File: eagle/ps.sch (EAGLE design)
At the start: 12 parts, among them J1 PIN2F061.100, J2 PIN2F061.100

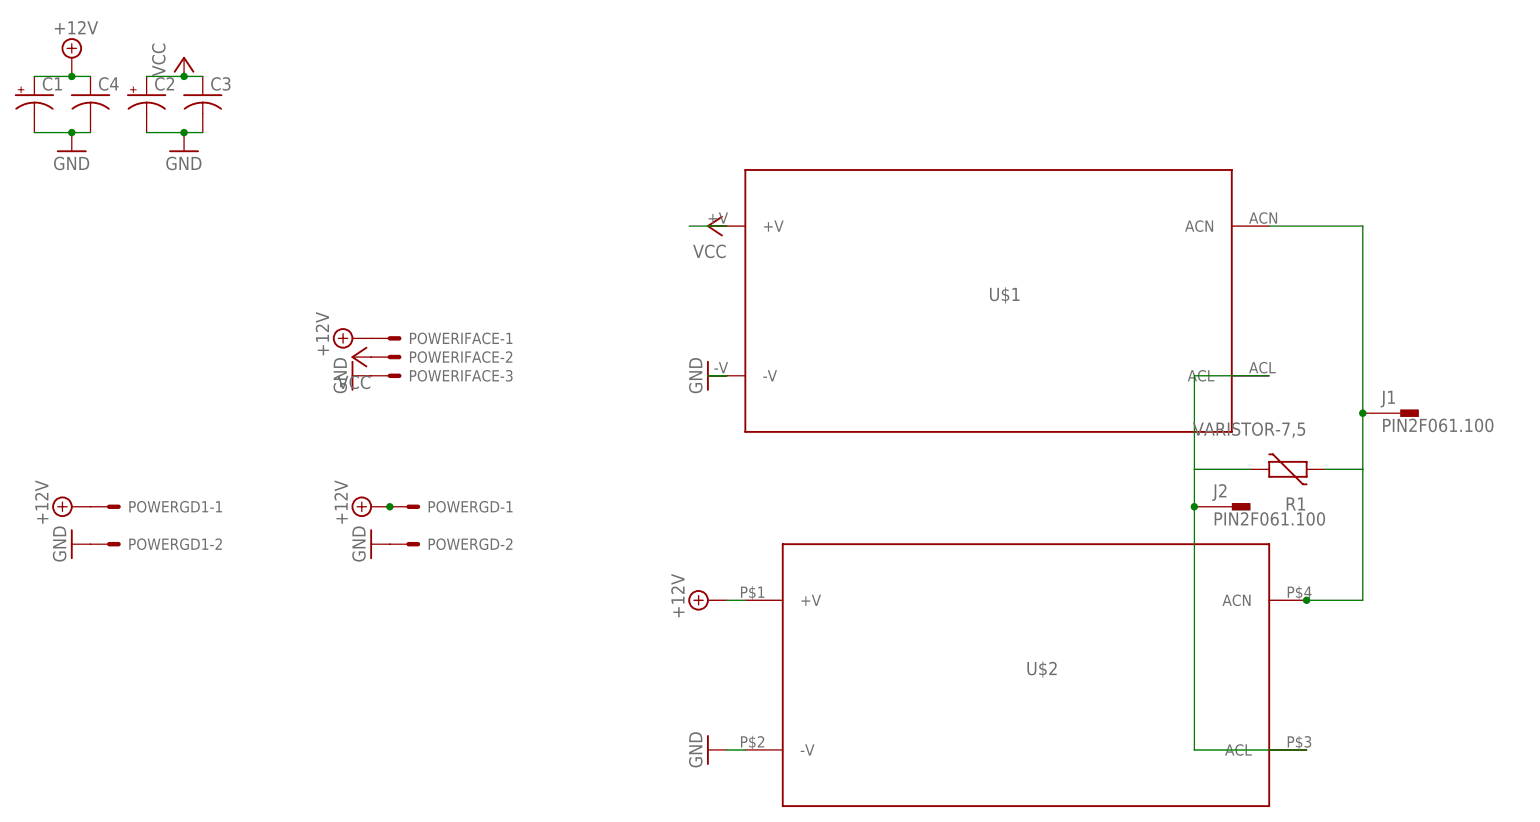
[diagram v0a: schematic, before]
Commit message: 3PS, 2 1kV in parallel
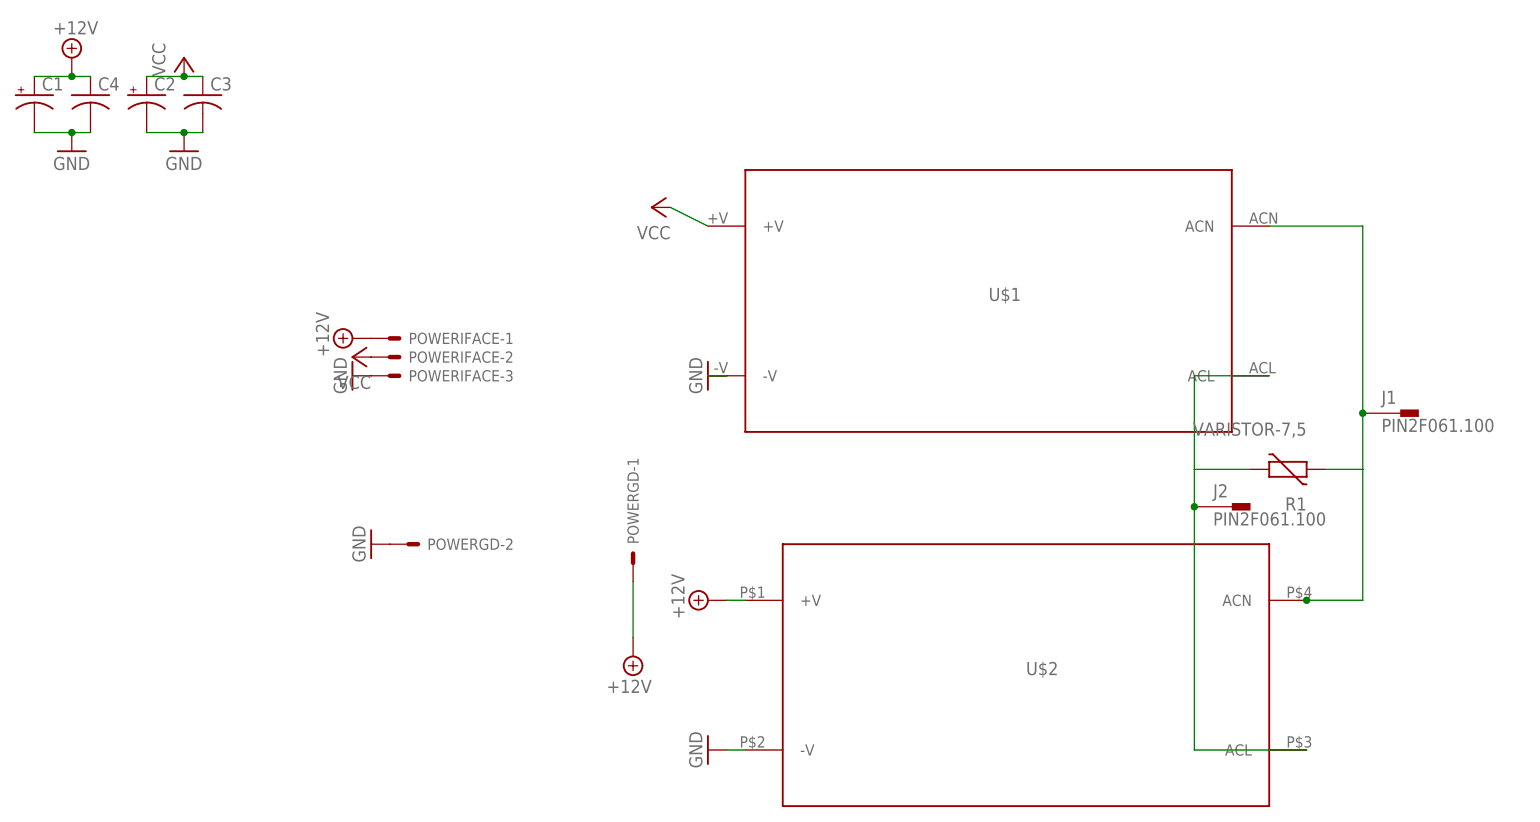
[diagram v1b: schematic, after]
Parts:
- removed POWERGD1: (no value), con-molex:KK-156-2
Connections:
- removed net +15V: C1.+, C4.1, POWERGD-1.S, POWERGD1-1.S, POWERIFACE-1.S, U$2.+V
- new net +12V: C1.+, C4.1, POWERGD-1.S, POWERIFACE-1.S, U$2.+V
- net GND: no longer POWERGD1-2.S
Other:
- moved on the sheet: POWERGD-1
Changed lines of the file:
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@@
 <part name="P+6" library="supply2" deviceset="+12V" device=""/>
 <part name="P+8" library="supply1" deviceset="VCC" device=""/>
-<part name="POWERGD1" library="con-molex" deviceset="KK-156-2" device=""/>
-<part name="P+9" library="supply2" deviceset="+12V" device=""/>
-<part name="GND8" library="supply1" deviceset="GND" device=""/>
 <part name="R1" library="varistor" deviceset="VARISTOR" device="-7,5"/>
 <part name="U$2" library="meanwell" deviceset="IRM-60-12" device=""/>
@@
 <instances>
 <instance part="U$1" gate="G$1" x="35.56" y="71.12"/>
-<instance part="P+1" gate="VCC" x="-2.54" y="81.28" rot="R90"/>
+<instance part="P+1" gate="VCC" x="-10.16" y="83.82" rot="R90"/>
 <instance part="P+2" gate="+12V" x="-2.54" y="30.48" rot="R90"/>
 <instance part="GND1" gate="1" x="-2.54" y="60.96" rot="R270"/>
@@
 <instance part="POWERIFACE" gate="-2" x="-45.72" y="63.5"/>
 <instance part="POWERIFACE" gate="-3" x="-45.72" y="60.96"/>
-<instance part="POWERGD" gate="-1" x="-43.18" y="43.18"/>
+<instance part="POWERGD" gate="-1" x="-12.7" y="35.56" rot="R90"/>
 <instance part="POWERGD" gate="-2" x="-43.18" y="38.1"/>
 <instance part="P+3" gate="VCC" x="-50.8" y="63.5" rot="R90"/>
 <instance part="P+4" gate="+12V" x="-50.8" y="66.04" rot="R90"/>
-<instance part="P+5" gate="+12V" x="-48.26" y="43.18" rot="R90"/>
+<instance part="P+5" gate="+12V" x="-12.7" y="22.86" rot="R180"/>
 <instance part="GND3" gate="1" x="-50.8" y="60.96" rot="R270"/>
 <instance part="GND4" gate="1" x="-48.26" y="38.1" rot="R270"/>
@@
 <instance part="P+6" gate="+12V" x="-88.9" y="104.14"/>
 <instance part="P+8" gate="VCC" x="-73.66" y="104.14"/>
-<instance part="POWERGD1" gate="-1" x="-83.82" y="43.18"/>
-<instance part="POWERGD1" gate="-2" x="-83.82" y="38.1"/>
-<instance part="P+9" gate="+12V" x="-88.9" y="43.18" rot="R90"/>
-<instance part="GND8" gate="1" x="-88.9" y="38.1" rot="R270"/>
 <instance part="R1" gate="G$1" x="76.2" y="48.26" rot="R180"/>
 <instance part="U$2" gate="IRM-60-12" x="40.64" y="20.32"/>
@@
 <nets>
 <net name="VCC" class="0">
-<segment>
-<pinref part="U$1" gate="G$1" pin="+V"/>
-<pinref part="P+1" gate="VCC" pin="VCC"/>
-<wire x1="-2.54" y1="81.28" x2="0" y2="81.28" width="0.1524" layer="91"/>
-<wire x1="-5.08" y1="81.28" x2="-2.54" y2="81.28" width="0.1524" layer="91"/>
-</segment>
 <segment>
 <pinref part="POWERIFACE" gate="-2" pin="S"/>
@@
 <junction x="-73.66" y="101.6"/>
 </segment>
+<segment>
+<pinref part="U$1" gate="G$1" pin="+V"/>
+<pinref part="P+1" gate="VCC" pin="VCC"/>
+<wire x1="-7.62" y1="83.82" x2="-2.54" y2="81.28" width="0.1524" layer="91"/>
+</segment>
 </net>
-<net name="+15V" class="0">
-<segment>
-<pinref part="P+2" gate="+12V" pin="+12V"/>
-<pinref part="U$2" gate="IRM-60-12" pin="+V"/>
-<wire x1="2.54" y1="30.48" x2="0" y2="30.48" width="0.1524" layer="91"/>
-</segment>
+<net name="+12V" class="0">
 <segment>
 <pinref part="POWERIFACE" gate="-1" pin="S"/>
@@
 <pinref part="POWERGD" gate="-1" pin="S"/>
 <pinref part="P+5" gate="+12V" pin="+12V"/>
-<junction x="-45.72" y="43.18"/>
+<wire x1="-12.7" y1="33.02" x2="-12.7" y2="25.4" width="0.1524" layer="91"/>
 </segment>
 <segment>
@@
 </segment>
 <segment>
-<pinref part="POWERGD1" gate="-1" pin="S"/>
-<pinref part="P+9" gate="+12V" pin="+12V"/>
+<pinref part="U$2" gate="IRM-60-12" pin="+V"/>
+<pinref part="P+2" gate="+12V" pin="+12V"/>
+<wire x1="0" y1="30.48" x2="2.54" y2="30.48" width="0.1524" layer="91"/>
 </segment>
 </net>
@@
 <junction x="-73.66" y="93.98"/>
 </segment>
-<segment>
-<pinref part="POWERGD1" gate="-2" pin="S"/>
-<pinref part="GND8" gate="1" pin="GND"/>
-</segment>
 </net>

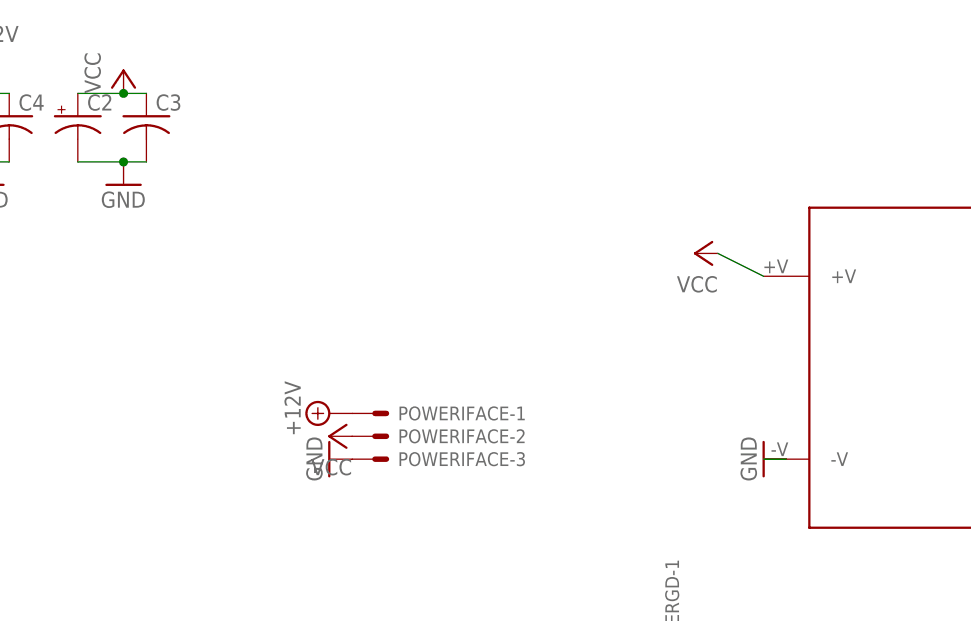
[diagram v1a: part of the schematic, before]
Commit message: capacitor bank
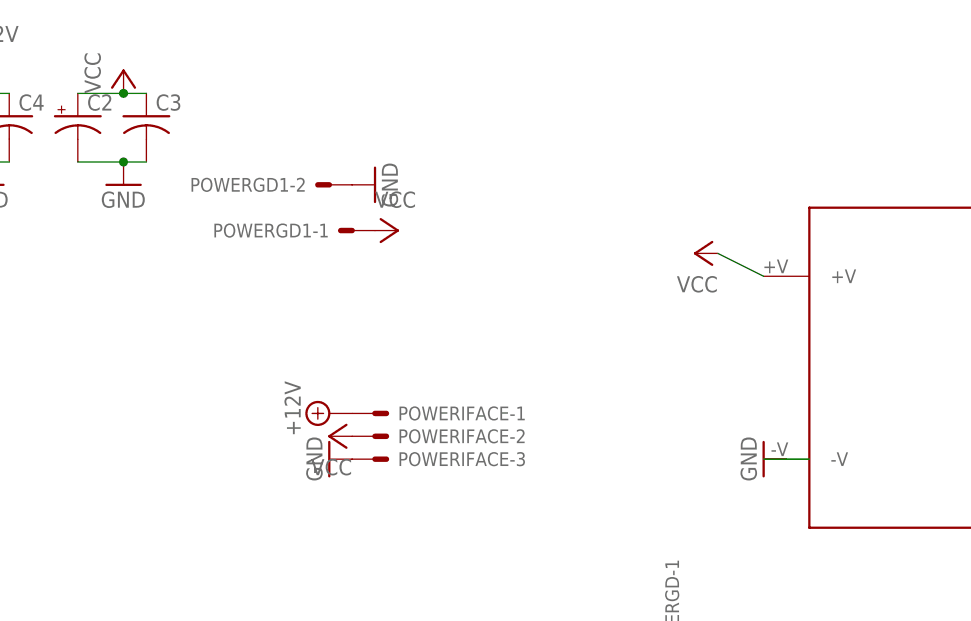
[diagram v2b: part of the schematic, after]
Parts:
- added POWERGD1: (no value), con-molex:KK-156-2
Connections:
- net GND: now also POWERGD1-2.S
- net VCC: now also POWERGD1-1.S
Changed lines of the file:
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@@
 <part name="R1" library="varistor" deviceset="VARISTOR" device="-7,5"/>
 <part name="U$2" library="meanwell" deviceset="IRM-60-12" device=""/>
+<part name="POWERGD1" library="con-molex" deviceset="KK-156-2" device=""/>
+<part name="GND5" library="supply1" deviceset="GND" device=""/>
+<part name="P+7" library="supply1" deviceset="VCC" device=""/>
 </parts>
 <sheets>
@@
 <instance part="R1" gate="G$1" x="76.2" y="48.26" rot="R180"/>
 <instance part="U$2" gate="IRM-60-12" x="40.64" y="20.32"/>
+<instance part="POWERGD1" gate="-1" x="-48.26" y="86.36" rot="R180"/>
+<instance part="POWERGD1" gate="-2" x="-50.8" y="91.44" rot="R180"/>
+<instance part="GND5" gate="1" x="-45.72" y="91.44" rot="R90"/>
+<instance part="P+7" gate="VCC" x="-43.18" y="86.36" rot="R270"/>
 </instances>
 <busses>
@@
 <pinref part="P+1" gate="VCC" pin="VCC"/>
 <wire x1="-7.62" y1="83.82" x2="-2.54" y2="81.28" width="0.1524" layer="91"/>
+</segment>
+<segment>
+<pinref part="POWERGD1" gate="-1" pin="S"/>
+<pinref part="P+7" gate="VCC" pin="VCC"/>
 </segment>
 </net>
@@
 <pinref part="GND1" gate="1" pin="GND"/>
 <wire x1="-2.54" y1="60.96" x2="0" y2="60.96" width="0.1524" layer="91"/>
+<wire x1="0" y1="60.96" x2="2.54" y2="60.96" width="0.1524" layer="91"/>
 </segment>
 <segment>
@@
 <junction x="-73.66" y="93.98"/>
 </segment>
+<segment>
+<pinref part="POWERGD1" gate="-2" pin="S"/>
+<pinref part="GND5" gate="1" pin="GND"/>
+</segment>
 </net>
